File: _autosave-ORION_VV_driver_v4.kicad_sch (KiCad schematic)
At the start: 165 parts, among them J1 Conn_01x01, J10 Conn_01x01, J11 Conn_01x02, J12 Conn_01x05, J13 Conn_01x05, J14 Conn_01x01, J15 Conn_01x02, J16 Conn_01x01, J17 Conn_01x01, J18 Conn_01x01, J19 Conn_01x01, J2 Conn_01x04, J20 Conn_01x01, J21 Conn_01x01, J22 Conn_01x01, J23 Conn_01x01, J3 Conn_01x04, J4 Conn_01x06, J5 Conn_01x07, J6 Conn_01x07, J7 Conn_01x01, J8 Conn_01x01, J9 Conn_01x01, Q1 IRF8721PBF-1, Q10 IRF8721PBF-1, Q11 IRF8721PBF-1, Q12 IRF8721PBF-1, Q2 IRF8721PBF-1, Q3 IRF8721PBF-1, Q4 IRF8721PBF-1, Q5 IRF8721PBF-1, Q6 IRF8721PBF-1, Q7 IRF8721PBF-1, Q8 IRF8721PBF-1, Q9 IRF8721PBF-1, SW1 SW_Push, SW2 SW_Push, SW3 SW_Push, SW4 SW_Push, SW5 SW_Push, U1 BD9G101G, U2 L78L33_SOT89, U3 MAX3051, U5 ZXCT108x, U6 ZXCT108x, Y1 Resonator

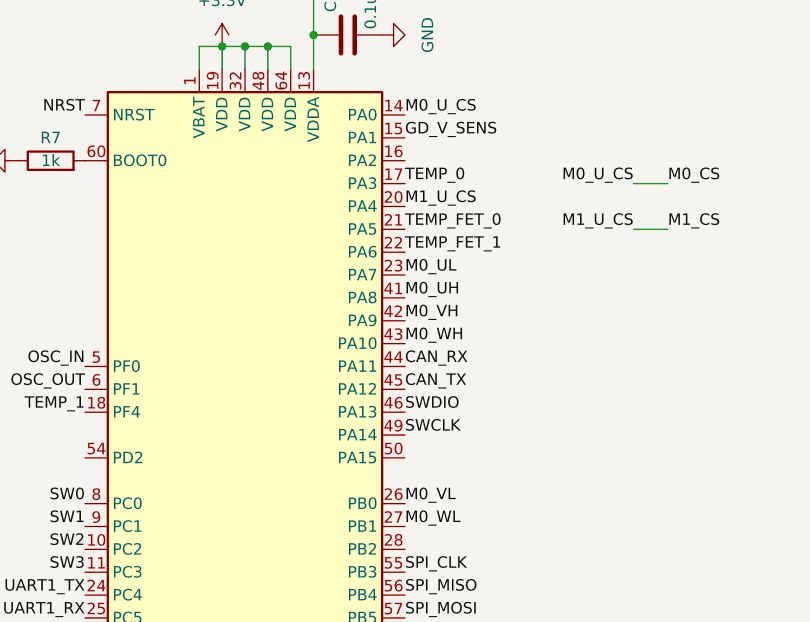
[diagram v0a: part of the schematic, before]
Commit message: 判別用シルク追加
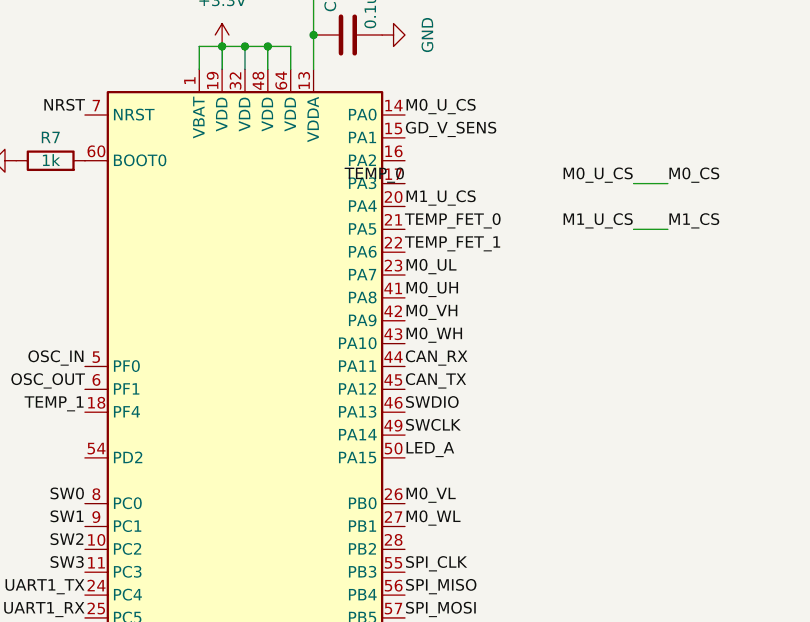
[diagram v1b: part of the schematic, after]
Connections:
- net LED_A: now reaches U4.50 (PA15)
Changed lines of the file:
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@@
     (effects (font (size 1.27 1.27)) (justify right bottom))
   )
-  (label "TEMP_0" (at 233.68 143.51 0)
-    (effects (font (size 1.27 1.27)) (justify left bottom))
+  (label "TEMP_0" (at 233.68 143.51 180)
+    (effects (font (size 1.27 1.27)) (justify right bottom))
   )
   (label "TEMP_1" (at 250.19 372.11 180)
@@
     (effects (font (size 1.27 1.27)) (justify left bottom))
   )
+  (label "LED_A" (at 233.68 173.99 0)
+    (effects (font (size 1.27 1.27)) (justify left bottom))
+  )
